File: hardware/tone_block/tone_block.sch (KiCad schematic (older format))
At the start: 31 parts, among them J1 I/O, J2 Conn 1, J3 Conn 2, Q1 2SC3324, Q2 2SC3324, U1 TLV170DBV

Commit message: WIP tone block
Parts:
- removed D1: CUS551V30,H3F, Diode_SMD:D_SOD-323, symbol Device:D_Schottky_ALT
- removed J2: Conn 1, cycfi_library:pin_socket_2x3p_1.00mm_smd_vertical, symbol Connector_Generic:Conn_02x03_Counter_Clockwise
- removed J3: Conn 2, cycfi_library:pin_socket_2x3p_1.00mm_smd_vertical, symbol Connector_Generic:Conn_02x03_Counter_Clockwise
- removed JP1: Coil Shunt, Jumper:SolderJumper-2_P1.3mm_Open_TrianglePad1.0x1.5mm, symbol Jumper:Jumper_2_Open
- removed Q1, Q2: 2SC3324, Package_TO_SOT_SMD:SOT-23, symbol cycfi_library:npn_bec
- removed R10, R11: 39k, Resistor_SMD:R_0402_1005Metric, symbol Device:R
- removed R12, R13: 180k, Resistor_SMD:R_0402_1005Metric, symbol Device:R
- removed R14: 91k, Resistor_SMD:R_0402_1005Metric, symbol Device:R
- removed R15: 10k, Resistor_SMD:R_0402_1005Metric, symbol Device:R
- removed R16: 4.7k, Resistor_SMD:R_0402_1005Metric, symbol Device:R
- removed R7: 1.5k, Resistor_SMD:R_0402_1005Metric, symbol Device:R
- removed R8: 100k, Resistor_SMD:R_0402_1005Metric, symbol Device:R
- removed R9: 51k, Resistor_SMD:R_0402_1005Metric, symbol Device:R
- removed U1: TLV170DBV, Package_TO_SOT_SMD:SOT-23-5, symbol cycfi_library:TLV170DBV
- added C4: 104nF, Capacitor_SMD:C_0402_1005Metric, symbol Device:C
- added L1: 80mH, cycfi_library:tb_inductor, symbol pspice:INDUCTOR
- added SW1: RS32716R, cycfi_library:RS32716, symbol Switch:SW_Coded_SH-7050
- added SW2: RS32716C, cycfi_library:RS32716, symbol Switch:SW_Coded_SH-7050
- C1: value 4.5uF -> 13nF; footprint Capacitor_SMD:C_0603_1608Metric -> Capacitor_SMD:C_0402_1005Metric
- C2: value 0.1uF -> 26nF
- C3: value 10uF -> 52nF; footprint Capacitor_SMD:C_0603_1608Metric -> Capacitor_SMD:C_0402_1005Metric
- R1: value 100k -> 1280
- R2: value 51k -> 640
- R3: value 39k -> 320
- R4: value 1.5k -> 160
- R5: value 1.5k -> 80
- R6: value 39k -> 4.7k
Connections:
- net labels added: ext_cap, in
- net labels removed: V+, ext_coil+, ext_coil-, in+, in-
- wire segments 88 -> 63
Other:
- note added: "1, 2: External capacitor\n3, 4, 5: Main input and (pass thru) power\n"
- note added: "6, 7, 8: Main output and (pass thru) power\n9, 10: Mixing resistor shunt"
- note added: "Hex Coded Switch"
- note added: "Hex Coded Switch\n(Complementary)"
- note added: "Resonant Filter"
- note added: "Spectra Passive"
- note removed: "1, 2: External coil shunt\n3, 4, 5: External coil\n"
- note removed: "6, 7, 8: Main output and power\n9, 10: Mixing resistor shunt"
- note removed: "Main Coil"
- note removed: "Power Conditioning"
- note removed: "Redundant connections to the \ncoil via two small 1mm 2x3 \nconnectors for improved \nreliability."
- note removed: "Spectra Preamp"

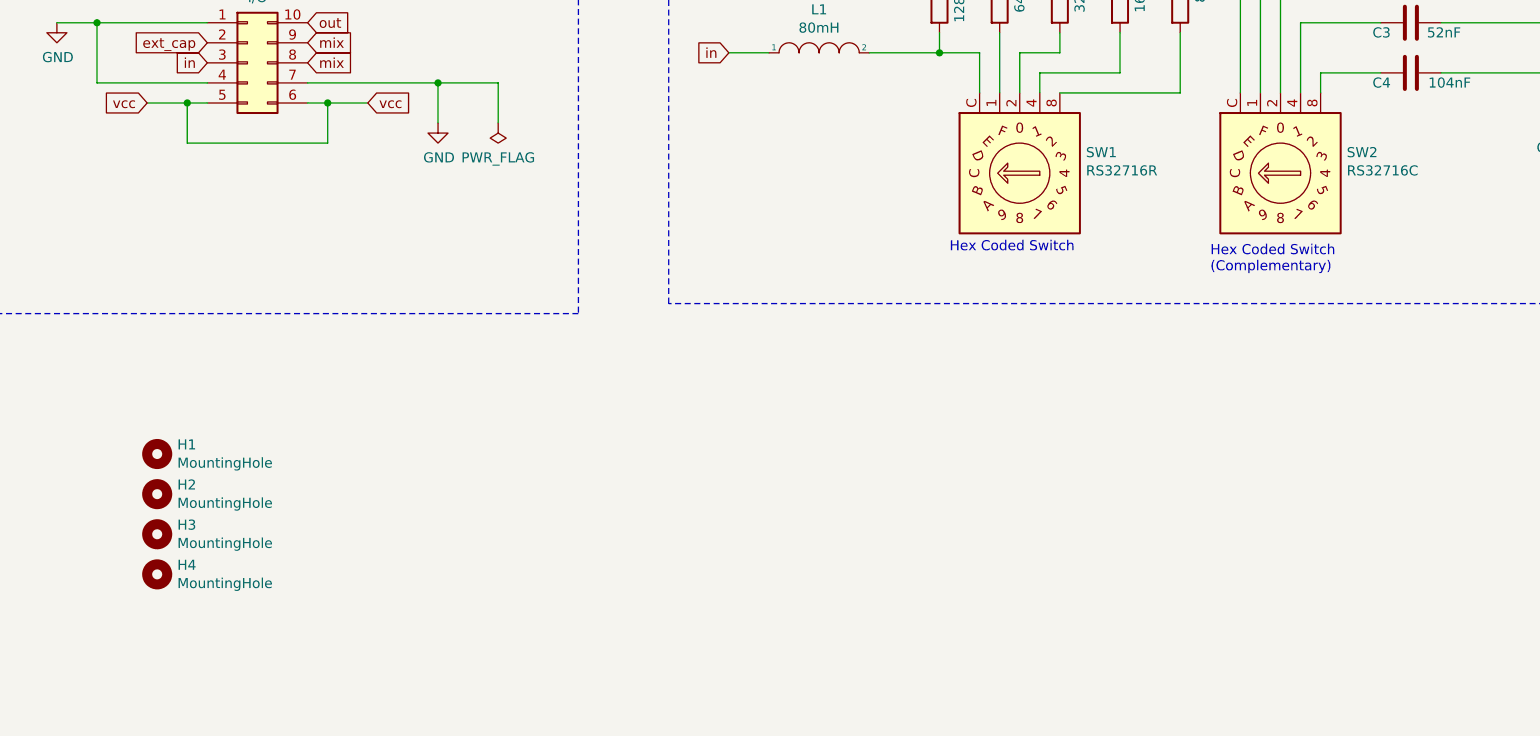
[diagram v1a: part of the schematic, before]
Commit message: fully routed
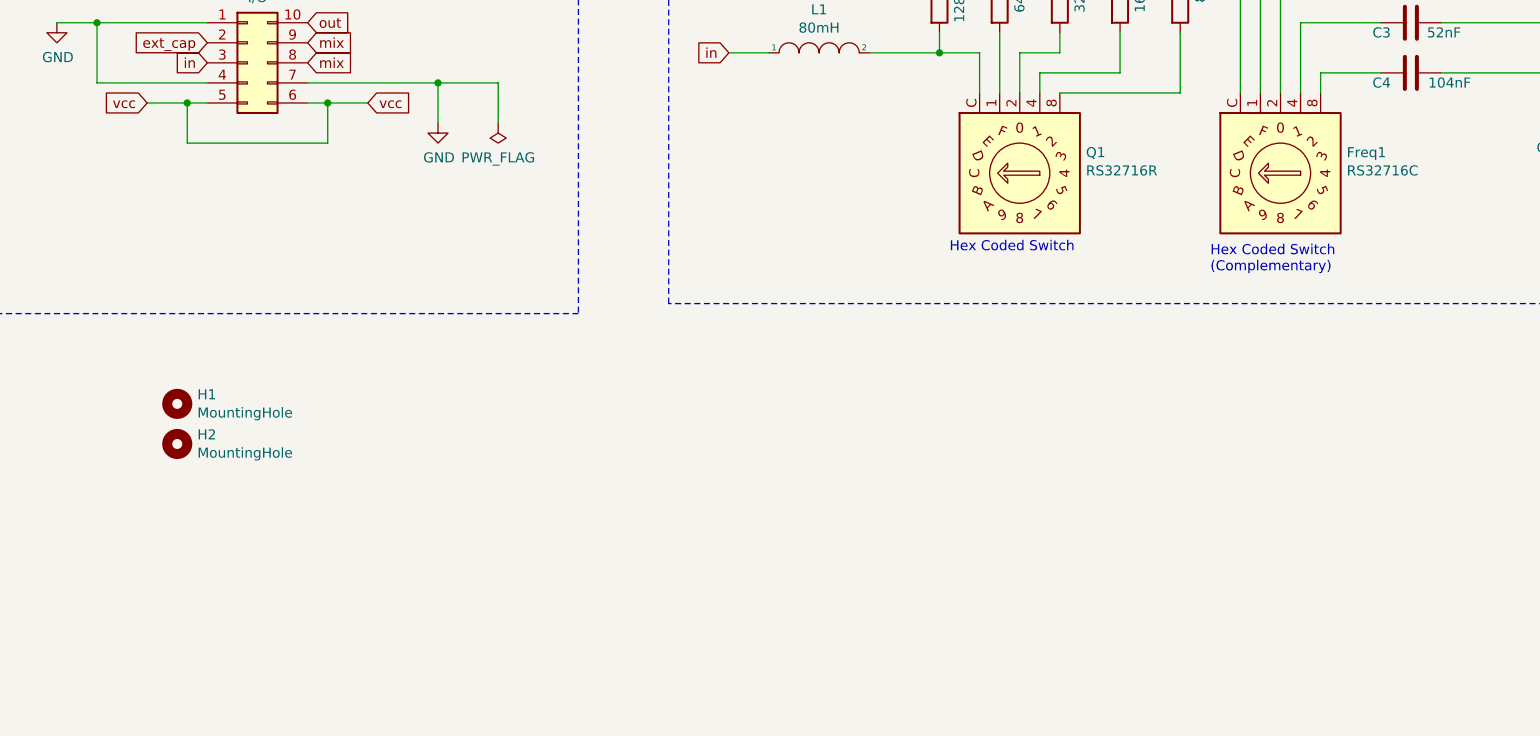
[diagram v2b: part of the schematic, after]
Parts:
- removed H3, H4: MountingHole, cycfi_library:mounting_hole_st1.9, symbol Mechanical:MountingHole
- H1, H2: footprint cycfi_library:mounting_hole_st1.9 -> cycfi_library:self_clinching_m3
- J1: footprint cycfi_library:pin_header_2x5p_2.54mm_smd_horizontal -> cycfi_library:pin_header_2x05_P2.54mm_vertical
- renumbered SW2 to Freq1, SW1 to Q1
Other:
- moved on the sheet: H1, H2
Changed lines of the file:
@@
 Resonant Filter
 $Comp
-L Switch:SW_Coded_SH-7050 SW1
+L Switch:SW_Coded_SH-7050 Q1
 U 1 1 611CF2DA
 P 7000 4550
-F 0 "SW1" V 7103 4220 50  0000 R CNN
+F 0 "Q1" V 7103 4220 50  0000 R CNN
 F 1 "RS32716R" V 7012 4220 50  0000 R CNN
 F 2 "cycfi_library:RS32716" H 6700 4100 50  0001 L CNN
@@
 Connection ~ 6600 3950
 $Comp
-L Switch:SW_Coded_SH-7050 SW2
+L Switch:SW_Coded_SH-7050 Freq1
 U 1 1 611D5413
 P 8300 4550
-F 0 "SW2" V 8403 4220 50  0000 R CNN
+F 0 "Freq1" V 8403 4220 50  0000 R CNN
 F 1 "RS32716C" V 8312 4220 50  0000 R CNN
 F 2 "cycfi_library:RS32716" H 8000 4100 50  0001 L CNN
@@
 F 0 "J1" H 3200 4417 50  0000 C CNN
 F 1 "I/O" H 3200 4326 50  0000 C CNN
-F 2 "cycfi_library:pin_header_2x5p_2.54mm_smd_horizontal" H 3150 4000 50  0001 C CNN
+F 2 "cycfi_library:pin_header_2x05_P2.54mm_vertical" H 3150 4000 50  0001 C CNN
 F 3 "~" H 3150 4000 50  0001 C CNN
 	1    3150 4000
@@
 L Mechanical:MountingHole H1
 U 1 1 61215F93
-P 2700 5950
-F 0 "H1" H 2800 5996 50  0000 L CNN
-F 1 "MountingHole" H 2800 5905 50  0000 L CNN
-F 2 "cycfi_library:mounting_hole_st1.9" H 2700 5950 50  0001 C CNN
-F 3 "~" H 2700 5950 50  0001 C CNN
-	1    2700 5950
+P 2800 5700
+F 0 "H1" H 2900 5746 50  0000 L CNN
+F 1 "MountingHole" H 2900 5655 50  0000 L CNN
+F 2 "cycfi_library:self_clinching_m3" H 2800 5700 50  0001 C CNN
+F 3 "~" H 2800 5700 50  0001 C CNN
+	1    2800 5700
 	1    0    0    -1
 $EndComp
@@
 L Mechanical:MountingHole H2
 U 1 1 61216B0B
-P 2700 6150
-F 0 "H2" H 2800 6196 50  0000 L CNN
-F 1 "MountingHole" H 2800 6105 50  0000 L CNN
-F 2 "cycfi_library:mounting_hole_st1.9" H 2700 6150 50  0001 C CNN
-F 3 "~" H 2700 6150 50  0001 C CNN
-	1    2700 6150
+P 2800 5900
+F 0 "H2" H 2900 5946 50  0000 L CNN
+F 1 "MountingHole" H 2900 5855 50  0000 L CNN
+F 2 "cycfi_library:self_clinching_m3" H 2800 5900 50  0001 C CNN
+F 3 "~" H 2800 5900 50  0001 C CNN
+	1    2800 5900
 	1    0    0    -1
 $EndComp
-$Comp
-L Mechanical:MountingHole H3
-U 1 1 61216C9C
-P 2700 6350
-F 0 "H3" H 2800 6396 50  0000 L CNN
-F 1 "MountingHole" H 2800 6305 50  0000 L CNN
-F 2 "cycfi_library:mounting_hole_st1.9" H 2700 6350 50  0001 C CNN
-F 3 "~" H 2700 6350 50  0001 C CNN
-	1    2700 6350
-	1    0    0    -1
-$EndComp
-$Comp
-L Mechanical:MountingHole H4
-U 1 1 61216E87
-P 2700 6550
-F 0 "H4" H 2800 6596 50  0000 L CNN
-F 1 "MountingHole" H 2800 6505 50  0000 L CNN
-F 2 "cycfi_library:mounting_hole_st1.9" H 2700 6550 50  0001 C CNN
-F 3 "~" H 2700 6550 50  0001 C CNN
-	1    2700 6550
-	1    0    0    -1
-$EndComp

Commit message: Fix mistake
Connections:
- net out is gone; now on net ext_cap: Freq1.C, J1.10 (Pin_10), R1.1, R2.1, R3.1, R4.1, R5.1, R6.1
- net ext_cap: no longer C1.1, Freq1.1
- new net: C1.1, Freq1.1
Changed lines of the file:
@@
 	7800 2700 8100 2700
 Wire Wire Line
-	8100 4150 8100 2700
+	8100 4150 8100 2950
 Connection ~ 8100 2700
 Wire Wire Line
@@
 Text GLabel 9300 2950 2    50   Input ~ 0
 ext_cap
-Wire Wire Line
-	9300 2950 8200 2950
-Wire Wire Line
-	8200 2950 8200 3300
-Connection ~ 8200 3300
 $Comp
 L Connector_Generic:Conn_02x05_Counter_Clockwise J1
@@
 	1    0    0    -1
 $EndComp
+Wire Wire Line
+	8100 2950 9300 2950
+Connection ~ 8100 2950
+Wire Wire Line
+	8100 2950 8100 2700
 $EndSCHEMATC

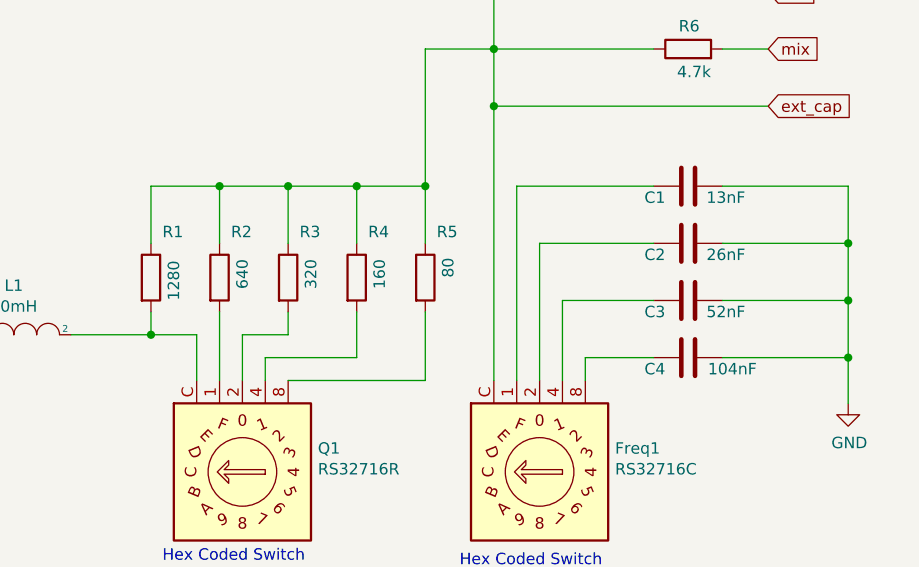
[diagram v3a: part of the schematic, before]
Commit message: Preamp and toneblock updates
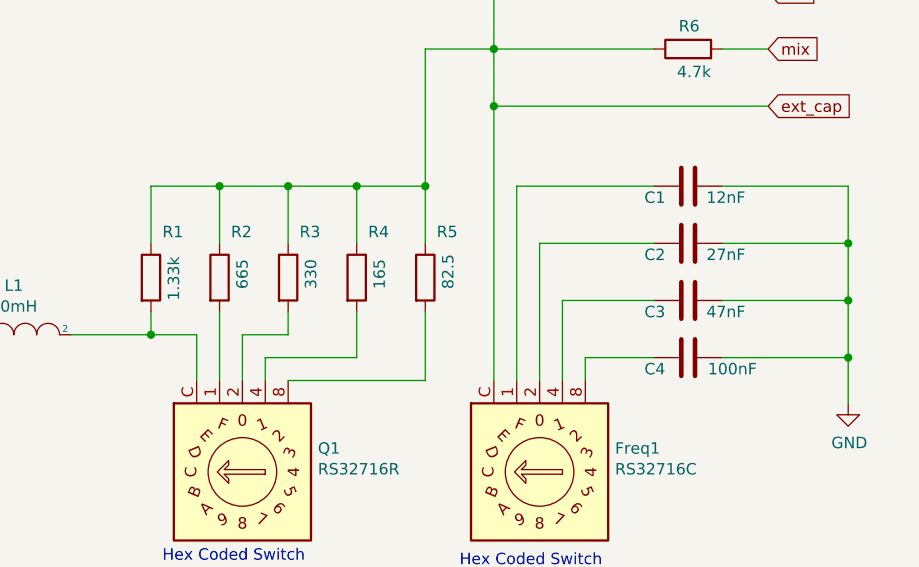
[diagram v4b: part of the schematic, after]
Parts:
- C1: value 13nF -> 12nF
- C2: value 26nF -> 27nF
- C3: value 52nF -> 47nF
- C4: value 104nF -> 100nF
- R1: value 1280 -> 1.33k
- R2: value 640 -> 665
- R3: value 320 -> 330
- R4: value 160 -> 165
- R5: value 80 -> 82.5
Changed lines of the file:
@@
 P 6900 3700
 F 0 "R2" H 6950 3900 50  0000 L CNN
-F 1 "640" V 7000 3650 50  0000 L CNN
+F 1 "665" V 7000 3650 50  0000 L CNN
 F 2 "Resistor_SMD:R_0402_1005Metric" V 6830 3700 50  0001 C CNN
 F 3 "~" H 6900 3700 50  0001 C CNN
@@
 P 7200 3700
 F 0 "R3" H 7250 3900 50  0000 L CNN
-F 1 "320" V 7300 3650 50  0000 L CNN
+F 1 "330" V 7300 3650 50  0000 L CNN
 F 2 "Resistor_SMD:R_0402_1005Metric" V 7130 3700 50  0001 C CNN
 F 3 "~" H 7200 3700 50  0001 C CNN
@@
 P 7500 3700
 F 0 "R4" H 7550 3900 50  0000 L CNN
-F 1 "160" V 7600 3650 50  0000 L CNN
+F 1 "165" V 7600 3650 50  0000 L CNN
 F 2 "Resistor_SMD:R_0402_1005Metric" V 7430 3700 50  0001 C CNN
 F 3 "~" H 7500 3700 50  0001 C CNN
@@
 P 7800 3700
 F 0 "R5" H 7850 3900 50  0000 L CNN
-F 1 "80" V 7900 3700 50  0000 L CNN
+F 1 "82.5" V 7900 3650 50  0000 L CNN
 F 2 "Resistor_SMD:R_0402_1005Metric" V 7730 3700 50  0001 C CNN
 F 3 "~" H 7800 3700 50  0001 C CNN
@@
 P 6600 3700
 F 0 "R1" H 6650 3900 50  0000 L CNN
-F 1 "1280" V 6700 3600 50  0000 L CNN
+F 1 "1.33k" V 6700 3600 50  0000 L CNN
 F 2 "Resistor_SMD:R_0402_1005Metric" V 6530 3700 50  0001 C CNN
 F 3 "~" H 6600 3700 50  0001 C CNN
@@
 P 8950 3800
 F 0 "C3" V 8900 3700 50  0000 R CNN
-F 1 "52nF" V 8900 4050 50  0000 R CNN
+F 1 "47nF" V 8900 4050 50  0000 R CNN
 F 2 "Capacitor_SMD:C_0402_1005Metric" H 8988 3650 50  0001 C CNN
 F 3 "~" H 8950 3800 50  0001 C CNN
@@
 P 8950 4050
 F 0 "C4" V 8900 3950 50  0000 R CNN
-F 1 "104nF" V 8900 4350 50  0000 R CNN
+F 1 "100nF" V 8900 4350 50  0000 R CNN
 F 2 "Capacitor_SMD:C_0402_1005Metric" H 8988 3900 50  0001 C CNN
 F 3 "~" H 8950 4050 50  0001 C CNN
@@
 P 8950 3550
 F 0 "C2" V 8900 3450 50  0000 R CNN
-F 1 "26nF" V 8900 3800 50  0000 R CNN
+F 1 "27nF" V 8900 3800 50  0000 R CNN
 F 2 "Capacitor_SMD:C_0402_1005Metric" H 8988 3400 50  0001 C CNN
 F 3 "~" H 8950 3550 50  0001 C CNN
@@
 P 8950 3300
 F 0 "C1" V 9000 3400 50  0000 L CNN
-F 1 "13nF" V 9000 3050 50  0000 L CNN
+F 1 "12nF" V 9000 3050 50  0000 L CNN
 F 2 "Capacitor_SMD:C_0402_1005Metric" H 8988 3150 50  0001 C CNN
 F 3 "~" H 8950 3300 50  0001 C CNN
